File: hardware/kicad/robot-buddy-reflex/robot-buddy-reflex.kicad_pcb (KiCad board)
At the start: 4 copper layers, 65 x 60 mm, 27 parts, among them J1 Motor A, J2 Motor B, J5 Qwiic, J6 HC-SR04, J7 E-Stop, J8 PWR In, J9 UART/Pi, U1 Waveshare_ESP32-S3-Zero, U2 SparkFun_TB6612FNG_v2

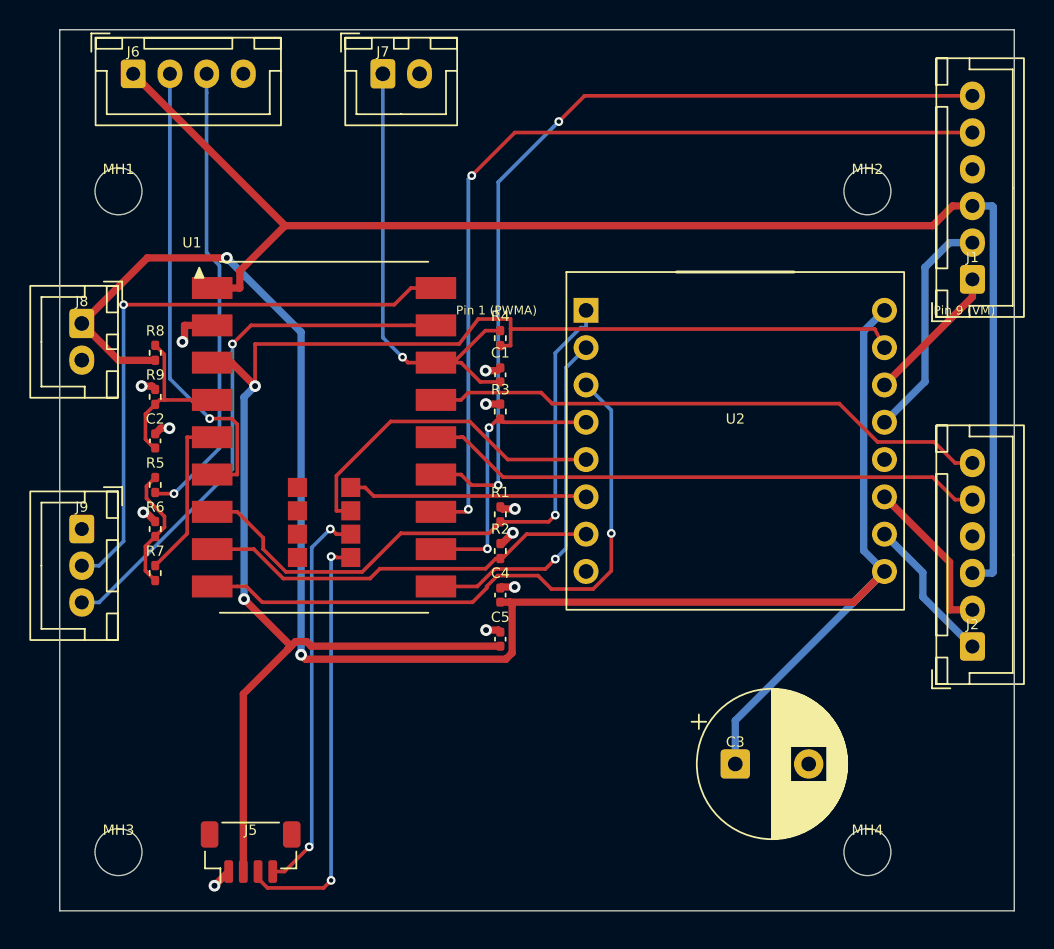
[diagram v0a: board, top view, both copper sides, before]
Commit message: kicad: fix DRC shorts, unconnected items, and dangling tracks
PCB DRC improved from 97 violations / 3 shorts / 2 unconnected / 2 dangling
to 90 violations / 0 shorts / 0 unconnected / 0 dangling.

Changes:
- /TRIG and /PWMA short (F.Cu): rerouted both nets through x=11.5 corridor
- /ESTOP and +3V3 short (F.Cu): replaced zig-zag with F.Cu stub + via (29.8,20.75) + B.Cu
  detour up to y=9.0 (above /ENC_LA B.Cu vertical at x=27.509)
- U1 pad 3 (+3V3) unconnected: added diagonal F.Cu track to (13.3,24.27)
- C1 pad 2 (GND) unconnected: added F.Cu stub + via (29.1,23.02) to GND plane
- Deleted orphan +3V3 segment (55.5,20.38)→(56.16,21.65)
- Trimmed +3V3 horizontal to x=55.007 and extended vertical to eliminate dangling end

Remaining 16 clearance violations are all minor (0.15–0.25 mm gap; no copper overlap).

Also move BIN1/BIN2 to GPIO38/39 (cluster pads 14/15 on flat-mount ESP32-S3-Zero)
and TRIG from GPIO21 (WS2812 LED conflict) to GPIO3.
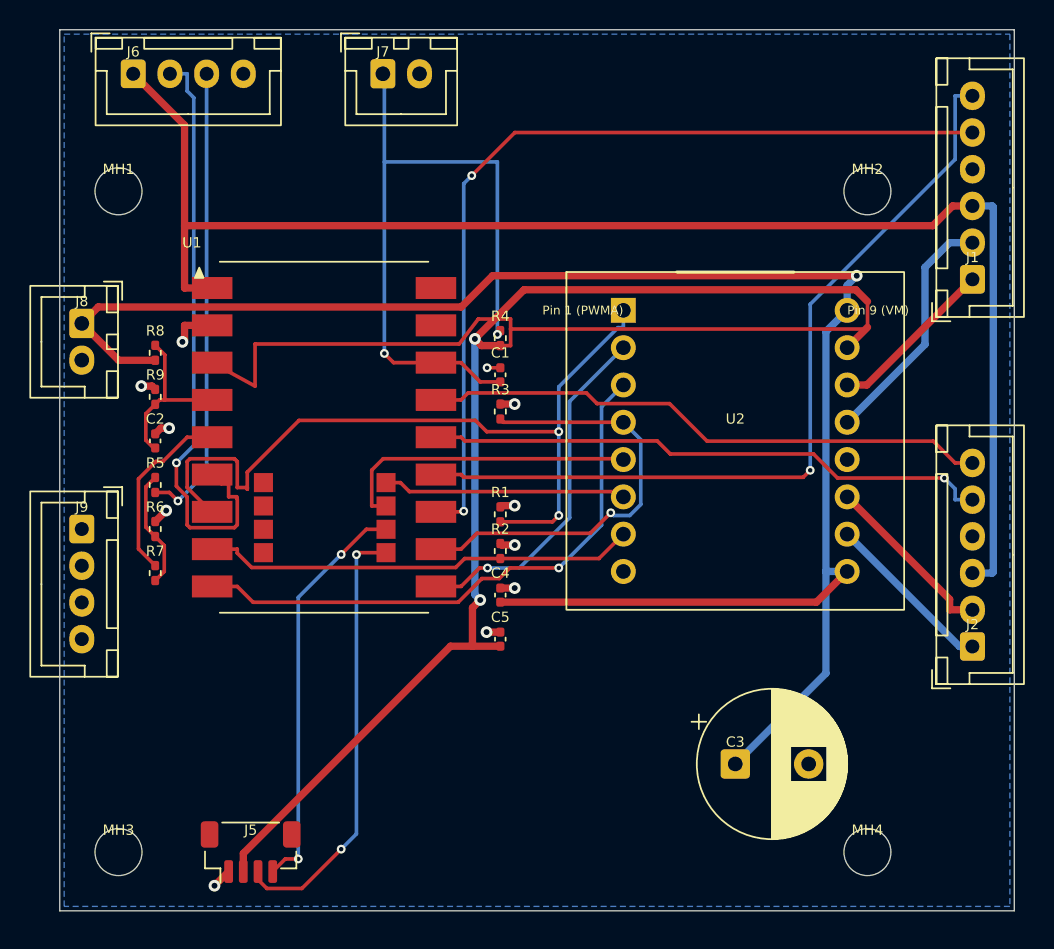
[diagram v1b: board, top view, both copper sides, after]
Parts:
- J9: footprint Connector_JST:JST_XH_B3B-XH-A_1x03_P2.50mm_Vertical -> Connector_JST:JST_XH_B4B-XH-A_1x04_P2.50mm_Vertical
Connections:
- J9 pad 1: GND -> unconnected-(J9-Pin_1-Pad1)
- J9 pad 2: /UART_TX -> unconnected-(J9-Pin_2-Pad2)
- J9 pad 3: /UART_RX -> unconnected-(J9-Pin_3-Pad3)
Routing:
- net /UART_TX: track 41.4 -> 0.00 mm, vias 1 -> 0
- net /UART_RX: track 36.9 -> 0.00 mm, vias 1 -> 0
- net +3V3: track 104.0 -> 131.3 mm
- net /ESTOP: track 31.3 -> 47.6 mm, vias 1 -> 2
- net /PWMA: track 42.1 -> 54.6 mm, vias 1 -> 2
- net /STBY: track 18.7 -> 29.9 mm, vias 2 -> 1
- net /TRIG: track 31.8 -> 41.2 mm
- net +BATT: track 128.4 -> 122.8 mm, vias 2 -> 1
- net /AIN1: track 42.7 -> 39.3 mm
- net /ENC_LB: track 59.9 -> 56.5 mm, vias 2 -> 1
- net +5V: track 97.2 -> 99.9 mm
- net /BIN1: track 23.0 -> 20.9 mm
- net /PWMB: track 27.5 -> 29.6 mm
- net /AO1: track 9.67 -> 11.5 mm
- net /BO1: track 10.1 -> 11.7 mm
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- added copper zone on B.Cu, net GND

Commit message: kicad: fix all DRC routing violations and export production gerbers
Resolved all routing violations on the 4-layer reflex board:
- Rerouted /TRIG to clear /PWMA diagonal (via x=12.1, right of U1 pad7)
- Rerouted +3V3 B.Cu with tiny jog at x=28.312 to clear /ENC_LA buried via
- Reverted /ECHO_MID from x=5.5 (shorted /ECHO_DIV) back to x=5.864
- Rerouted /ENC_RB with y=24.67 jog to clear GND via at (30.975,25.49)
- Rerouted /TRIG left section clear of U1 pad7 (/PWMA)
- Fixed U2 silk pin label text height 0.6→0.8mm
- Reverted /AIN1 to y=37.373 (impossible to clear both /AIN2 via and C4 GND pad;
  0.212mm gap is above PCBWay's 0.127mm manufacturing minimum)

Remaining DRC: 4 clearance violations at 0.212–0.241mm (KiCad rule 0.25mm;
PCBWay minimum 0.127mm — all manufacturable), 39 silk/lib warnings (non-manufacturing).

Exports: F/In1/In2/B.Cu, F/B.Mask, F/B.Paste, F/B.Silkscreen, Edge.Cuts gerbers
plus PTH and NPTH Excellon drill files, zipped for PCBWay upload.
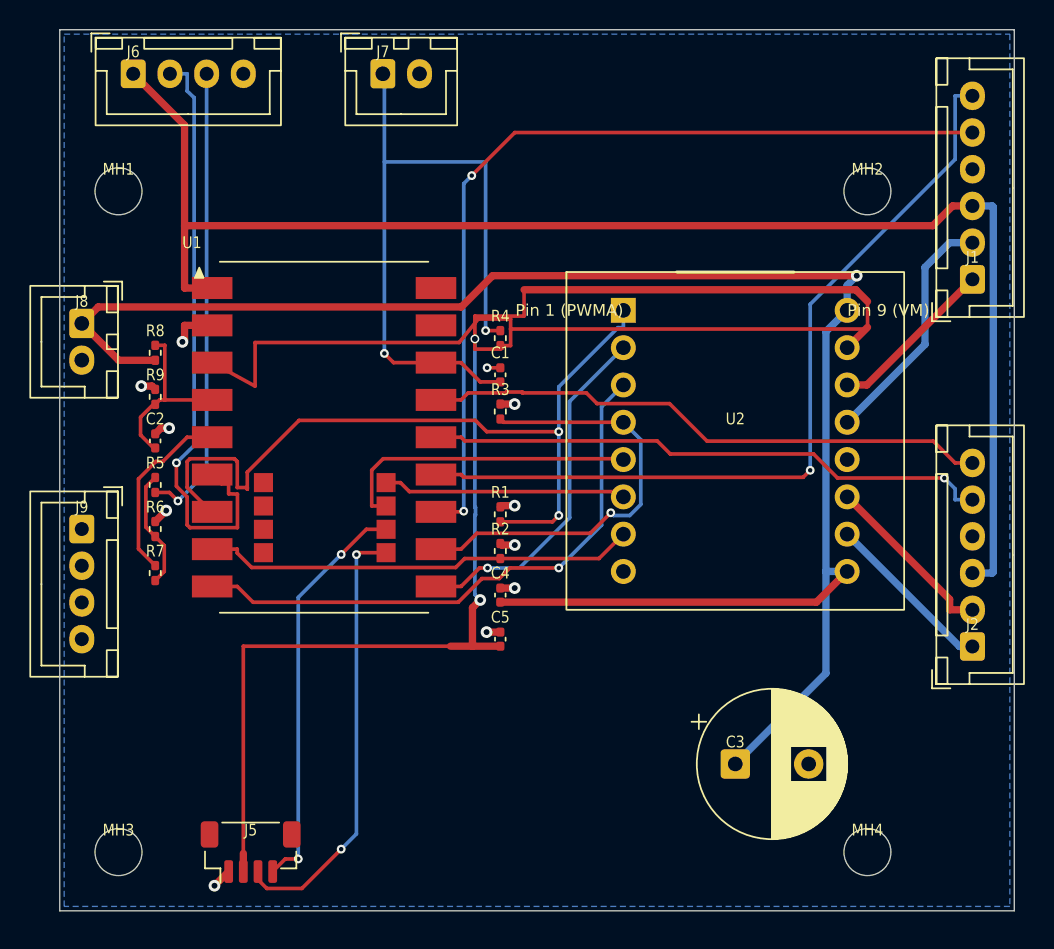
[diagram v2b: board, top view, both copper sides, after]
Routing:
- net +3V3: track 131.3 -> 142.4 mm
- net /BAT_SENSE: track 11.6 -> 12.4 mm

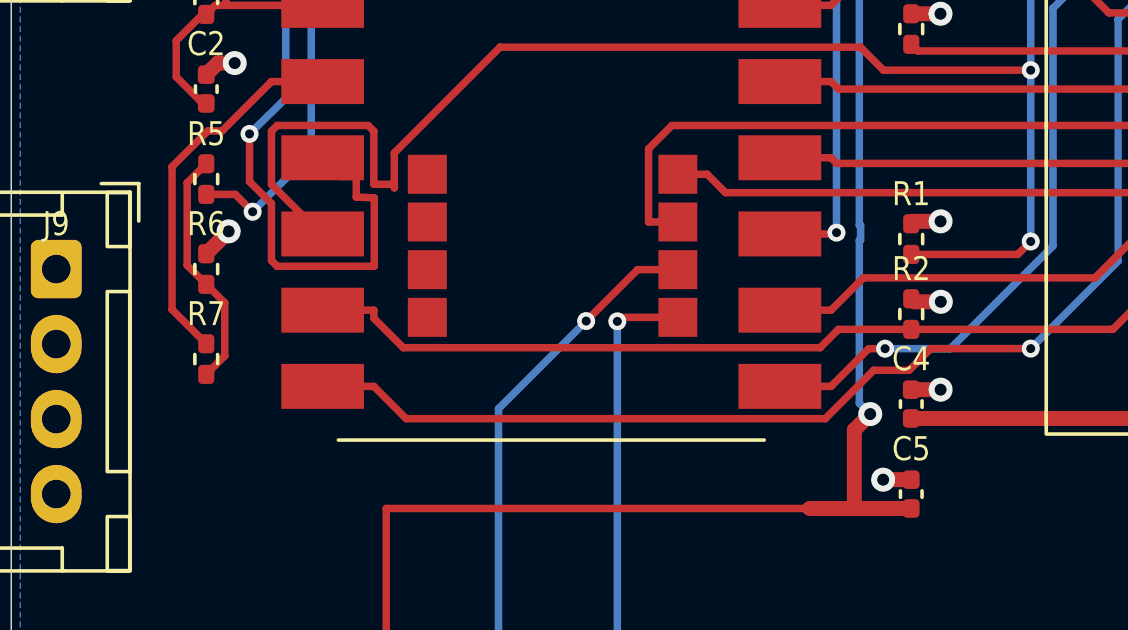
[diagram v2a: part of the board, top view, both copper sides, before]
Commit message: kicad: shift C4 and R6 to clear final clearance violations
Moved C4 down 0.1mm and R6 right 0.1mm to resolve the last 4 DRC
clearance violations:
- C4 (30.0,38.5→38.6): pad2 GND top edge now 37.81mm — 0.312mm gap
  to /AIN1 at y=37.373 (was 0.212mm, needed 0.250mm)
- R6 (6.5→6.6, 34.0): pad2 GND left edge now 6.33mm — 0.341mm gap
  to /ECHO_MID vertical at x=5.864 (was 0.241mm, needed 0.250mm)

Updated track endpoints to follow each pad: GND short-diagonal to
existing GND via, +BATT stub on C4 pad1, /ECHO_MID endpoint on R6 pad1.

DRC result: 0 clearance, 0 crossings, 0 shorts, 0 unconnected.
Remaining 49 violations are silk/lib only — non-manufacturing.

Regenerated gerbers at hardware/kicad/robot-buddy-reflex/gerbers/.
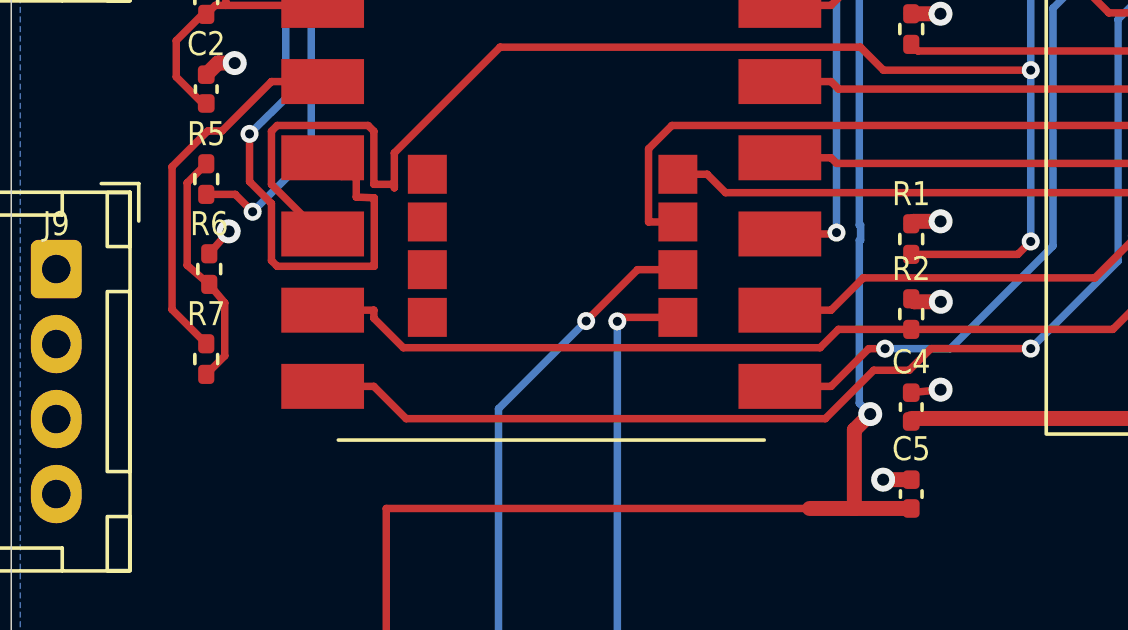
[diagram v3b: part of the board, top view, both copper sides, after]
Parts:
- moved C4 0.10 mm to (30.0, 38.6)
- moved R6 0.10 mm to (6.60, 34.0)
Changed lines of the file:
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@@
 	(footprint "Capacitor_SMD:C_0402_1005Metric"
 		(layer "F.Cu")
-		(at 30 38.5 90)
+		(at 30 38.6 90)
 		(descr "Capacitor SMD 0402 (1005 Metric), square (rectangular) end terminal, IPC-7351 nominal, (Body size source: IPC-SM-782 page 76, https://www.pcb-3d.com/wordpress/wp-content/uploads/ipc-sm-782a_amendment_1_and_2.pdf)")
 		(tags "capacitor")
@@
 	(footprint "Resistor_SMD:R_0402_1005Metric"
 		(layer "F.Cu")
-		(at 6.5 34 90)
+		(at 6.6 34 90)
 		(descr "Resistor SMD 0402 (1005 Metric), square (rectangular) end terminal, IPC-7351 nominal, (Body size source: IPC-SM-782 page 72, https://www.pcb-3d.com/wordpress/wp-content/uploads/ipc-sm-782a_amendment_1_and_2.pdf)")
 		(tags "resistor")
@@
 	)
 	(segment
+		(start 6.6 33.49)
+		(end 7.247 32.743)
+		(width 0.25)
+		(layer "F.Cu")
+		(net "GND")
+	)
+	(segment
 		(start 10.38 20.13)
 		(end 8.4983 20.13)
@@
 	)
 	(segment
-		(start 30 38.02)
-		(end 30.9785 38.02)
-		(width 0.5)
+		(start 30 38.12)
+		(end 30.979 38.02)
+		(width 0.25)
 		(layer "F.Cu")
 		(net "GND")
@@
 	)
 	(segment
-		(start 6.5 33.49)
-		(end 7.2468 32.7432)
-		(width 0.5)
-		(layer "F.Cu")
-		(net "GND")
-	)
-	(segment
 		(start 8.3532 21.2544)
 		(end 8.4983 21.1093)
@@
 	)
 	(segment
+		(start 30 38.98)
+		(end 30 39.08)
+		(width 0.25)
+		(layer "F.Cu")
+		(net "+BATT")
+	)
+	(segment
 		(start 29.4761 16.7491)
 		(end 54.2713 16.7491)
@@
 	)
 	(segment
-		(start 6.5 34.51)
-		(end 7.1171 35.1271)
-		(width 0.25)
-		(layer "F.Cu")
-		(net "/ECHO_MID")
-	)
-	(segment
 		(start 6.5 30.49)
 		(end 5.864 31.126)
@@
 	)
 	(segment
+		(start 6.6 34.51)
+		(end 7.117 35.127)
+		(width 0.25)
+		(layer "F.Cu")
+		(net "/ECHO_MID")
+	)
+	(segment
 		(start 5.864 33.874)
-		(end 6.5 34.51)
+		(end 6.6 34.51)
 		(width 0.25)
 		(layer "F.Cu")

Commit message: kicad: swap J6 HC-SR04 connector from JST XH to 2.54mm pin header
B4B-XH-A (2.5mm) replaced with PinHeader_1x04_P2.54mm_Vertical — HC-SR04
modules use 0.1" header pins directly so no adapter harness needed.
DRC clean (0 electrical errors).
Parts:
- J6: footprint Connector_JST:JST_XH_B4B-XH-A_1x04_P2.50mm_Vertical -> PinHeader_1x04_P2.54mm_Vertical
- turned J6 to 90 degrees

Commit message: hardware: add NeoPixel+power-LED circuit placement to buddy layout; regen STEP
J10 (XH 2-pin power LED), J11 (XH 3-pin NeoPixel), U3 (74LVC1G125 SOT-23-5),
R10/R11 (330Ω), C6 (100µF radial), C7 (100nF) placed in bottom-centre cluster.
Footprint count: 27 → 34.  STEP regenerated to match.
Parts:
- added C6: 100µF, Capacitor_THT:CP_Radial_D5.0mm_P2.00mm, F.Cu at (36.0, 50.0)
- added C7: 100n, Capacitor_SMD:C_0402_1005Metric, F.Cu at (28.0, 52.0)
- added J10: LED, Connector_JST:JST_XH_B2B-XH-A_1x02_P2.50mm_Vertical, F.Cu at (20.0, 57.0)
- added J11: NeoPixel, Connector_JST:JST_XH_B3B-XH-A_1x03_P2.50mm_Vertical, F.Cu at (30.0, 57.0)
- added R10: 330, Resistor_SMD:R_0402_1005Metric, F.Cu at (20.0, 52.0)
- added R11: 330, Resistor_SMD:R_0402_1005Metric, F.Cu at (24.0, 52.0)
- added U3: 74LVC1G125, Package_TO_SOT_SMD:SOT-23-5, F.Cu at (24.0, 46.0)
- J6: footprint PinHeader_1x04_P2.54mm_Vertical -> Connector_PinHeader_2.54mm:PinHeader_1x04_P2.54mm_Vertical
- moved C4 0.10 mm to (30.0, 38.5)
- moved R6 0.10 mm to (6.50, 34.0)
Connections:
- J9 pad 1: unconnected-(J9-Pin_1-Pad1) -> +5V
- J9 pad 2: unconnected-(J9-Pin_2-Pad2) -> GND
- J9 pad 3: unconnected-(J9-Pin_3-Pad3) -> /UART_TX
- J9 pad 4: unconnected-(J9-Pin_4-Pad4) -> /UART_RX
- U1 pad 11: unconnected-(U1-GPIO42-Pad11) -> /NEO_DATA
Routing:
- removed copper zone on B.Cu, net GND

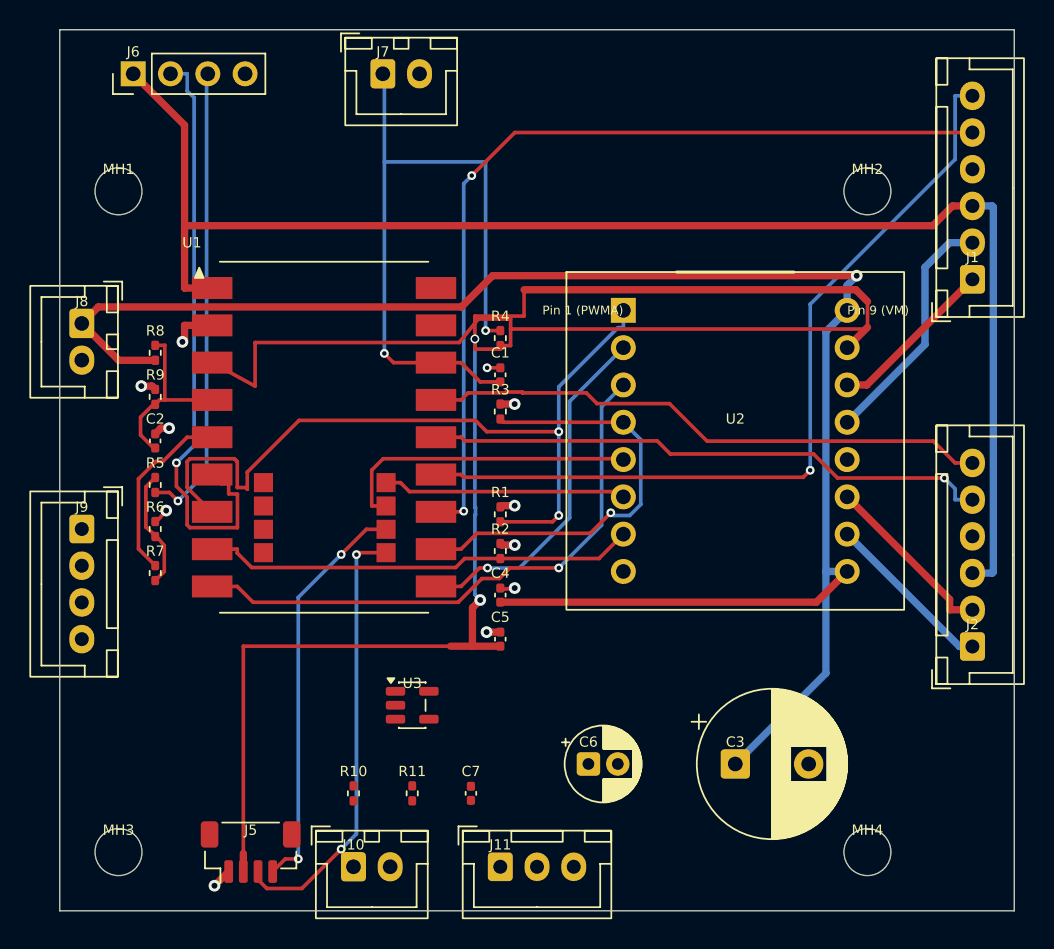
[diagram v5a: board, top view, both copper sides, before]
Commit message: kicad: route buddy board clean; regen gerbers with kicad-cli extensions
NeoPixel cluster shifted +5mm right in layout_pcb.py to clear SDA Qwiic
via conflict at (19.16, 55.80) with old J10 pad 1 at (20, 57).

route_pcb.py: POWER_W 0.50→0.40mm (R10/+5V clearance was 0.096mm <
JLCPCB 0.1mm minimum); +3V3 patch horizontal moved to y=21.15 (was 21.40,
too close to ESTOP via at (22.10, 22.04)); U2 pad-10 endpoint updated to
(53.62, 21.65) after NeoPixel shift moved U2 left.

Final DRC: 0 unconnected, 0 hard errors, worst clearance 0.129mm.

Gerbers regenerated with kicad-cli (extensions now .gtl/.gbl/.g1/.g2
etc. rather than .gbr); stale .gbr files removed; zip rebuilt clean.
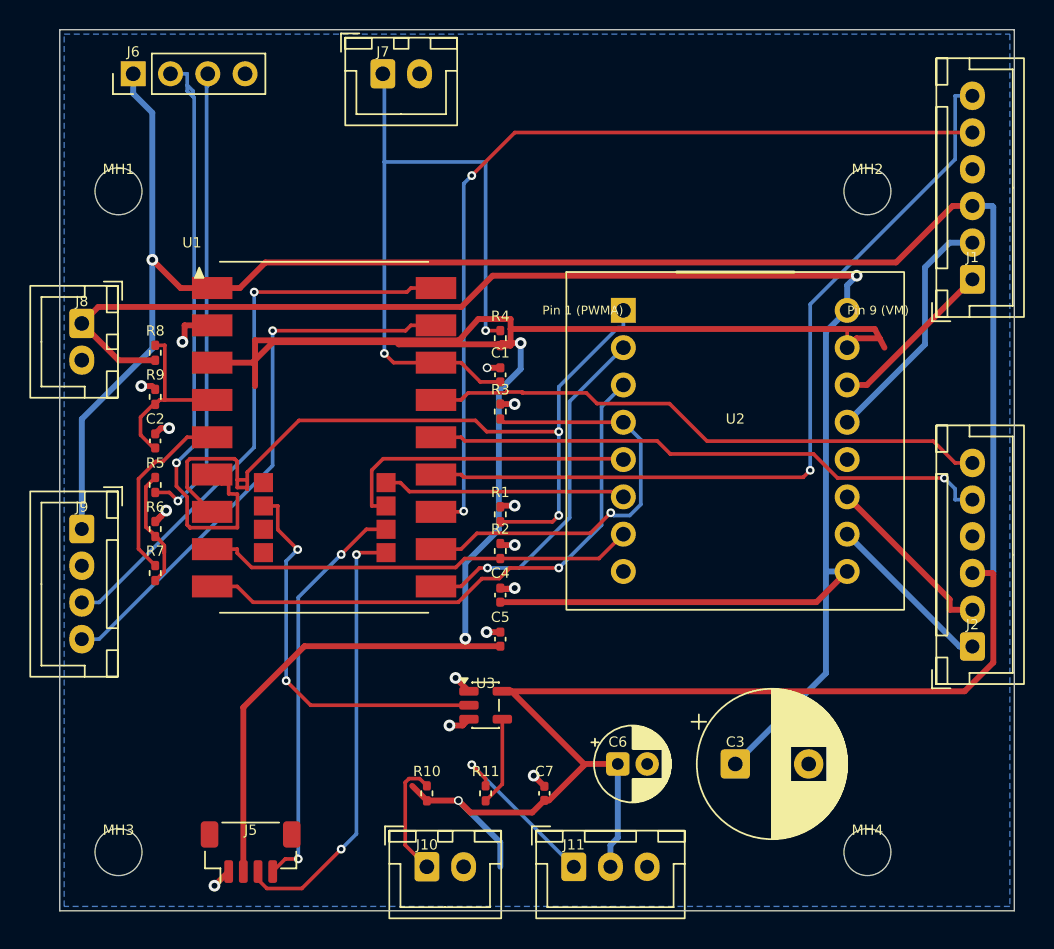
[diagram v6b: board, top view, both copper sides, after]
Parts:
- moved C7 5.00 mm to (33.0, 52.0)
- moved J10 5.00 mm to (25.0, 57.0)
- moved J11 5.00 mm to (35.0, 57.0)
- moved R10 5.00 mm to (25.0, 52.0)
- moved R11 5.00 mm to (29.0, 52.0)
- moved U3 5.00 mm to (29.0, 46.0)
- moved C6 2.00 mm to (38.0, 50.0)
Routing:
- net +5V: track 99.9 -> 198.2 mm, vias 0 -> 2
- net /UART_TX: track 0.00 -> 39.2 mm, vias 0 -> 1
- net /UART_RX: track 0.00 -> 38.4 mm, vias 0 -> 1
- net +3V3: track 142.4 -> 174.6 mm
- net /NEO_DATA: track 0.00 -> 26.9 mm, vias 0 -> 2
- net /NEO_DIN: track 0.00 -> 11.6 mm, vias 0 -> 1
- net /LED_A: track 0.00 -> 8.14 mm
- net /NEO_BUF: track 0.00 -> 6.03 mm
- net GND: track 13.4 -> 18.3 mm, vias 11 -> 14
- net /TRIG: track 41.4 -> 42.4 mm
- net /ECHO_IN: track 31.7 -> 32.6 mm
- net /PWMA: track 54.6 -> 55.3 mm
- net /ECHO_MID: track 8.06 -> 8.63 mm
- added copper zone on B.Cu, net GND
